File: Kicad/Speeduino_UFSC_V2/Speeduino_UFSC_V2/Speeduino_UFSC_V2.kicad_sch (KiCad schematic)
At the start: 1 part

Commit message: Add pdf
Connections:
- net MCU-A10: no longer names the net of A2.A10
- net MCU-A5: no longer names the net of A2.A5
- net MCU-A6: no longer names the net of A2.A6
- net MCU-A7: no longer names the net of A2.A7
- net MCU-A9: no longer names the net of A2.A9
- net MCU-D10: no longer names the net of A2.D10
- net MCU-D11: no longer names the net of A2.D11
- net MCU-D12: no longer names the net of A2.D12
- net MCU-D13: no longer names the net of A2.D13
- net MCU-D14: no longer names the net of A2.D14 (D14/TX3)
- net MCU-D15: no longer names the net of A2.D15 (D15/RX3)
- net MCU-D20: no longer names the net of A2.D20 (D20/SDA)
- net MCU-D21: no longer names the net of A2.D21 (D21/SCL)
- net MCU-D22: no longer names the net of A2.D22
- net MCU-D23: no longer names the net of A2.D23
- net MCU-D25: no longer names the net of A2.D25
- net MCU-D26: no longer names the net of A2.D26
- net MCU-D27: no longer names the net of A2.D27
- net MCU-D28: no longer names the net of A2.D28
- net MCU-D29: no longer names the net of A2.D29
- net MCU-D30: no longer names the net of A2.D30
- net MCU-D31: no longer names the net of A2.D31
- net MCU-D32: no longer names the net of A2.D32
- net MCU-D33: no longer names the net of A2.D33
- net MCU-D34: no longer names the net of A2.D34
- net MCU-D35: no longer names the net of A2.D35
- net MCU-D36: no longer names the net of A2.D36
- net MCU-D37: no longer names the net of A2.D37
- net MCU-D39: no longer names the net of A2.D39
- net MCU-D41: no longer names the net of A2.D41
- net MCU-D42: no longer names the net of A2.D42
- net MCU-D43: no longer names the net of A2.D43
- net MCU-D44: no longer names the net of A2.D44
- net MCU-D46: no longer names the net of A2.D46
- net MCU-D48: no longer names the net of A2.D48
- net MCU-D50: no longer names the net of A2.D50 (D50_MISO)
- net MCU-D52: no longer names the net of A2.D52 (D52_SCK)
- net MCU-D53: no longer names the net of A2.D53 (D53_CS)
- net MCU-D9: no longer names the net of A2.D9
- net MISO: no longer names the net of A2.MISO (SPI_MISO)
- net MOSI: no longer names the net of A2.MOSI (SPI_MOSI)
- net RESET: no longer names the net of A2.RST1 (RESET)
- net SCLK: no longer names the net of A2.SCK (SPI_SCK)
- no-connect marks 3 -> 55

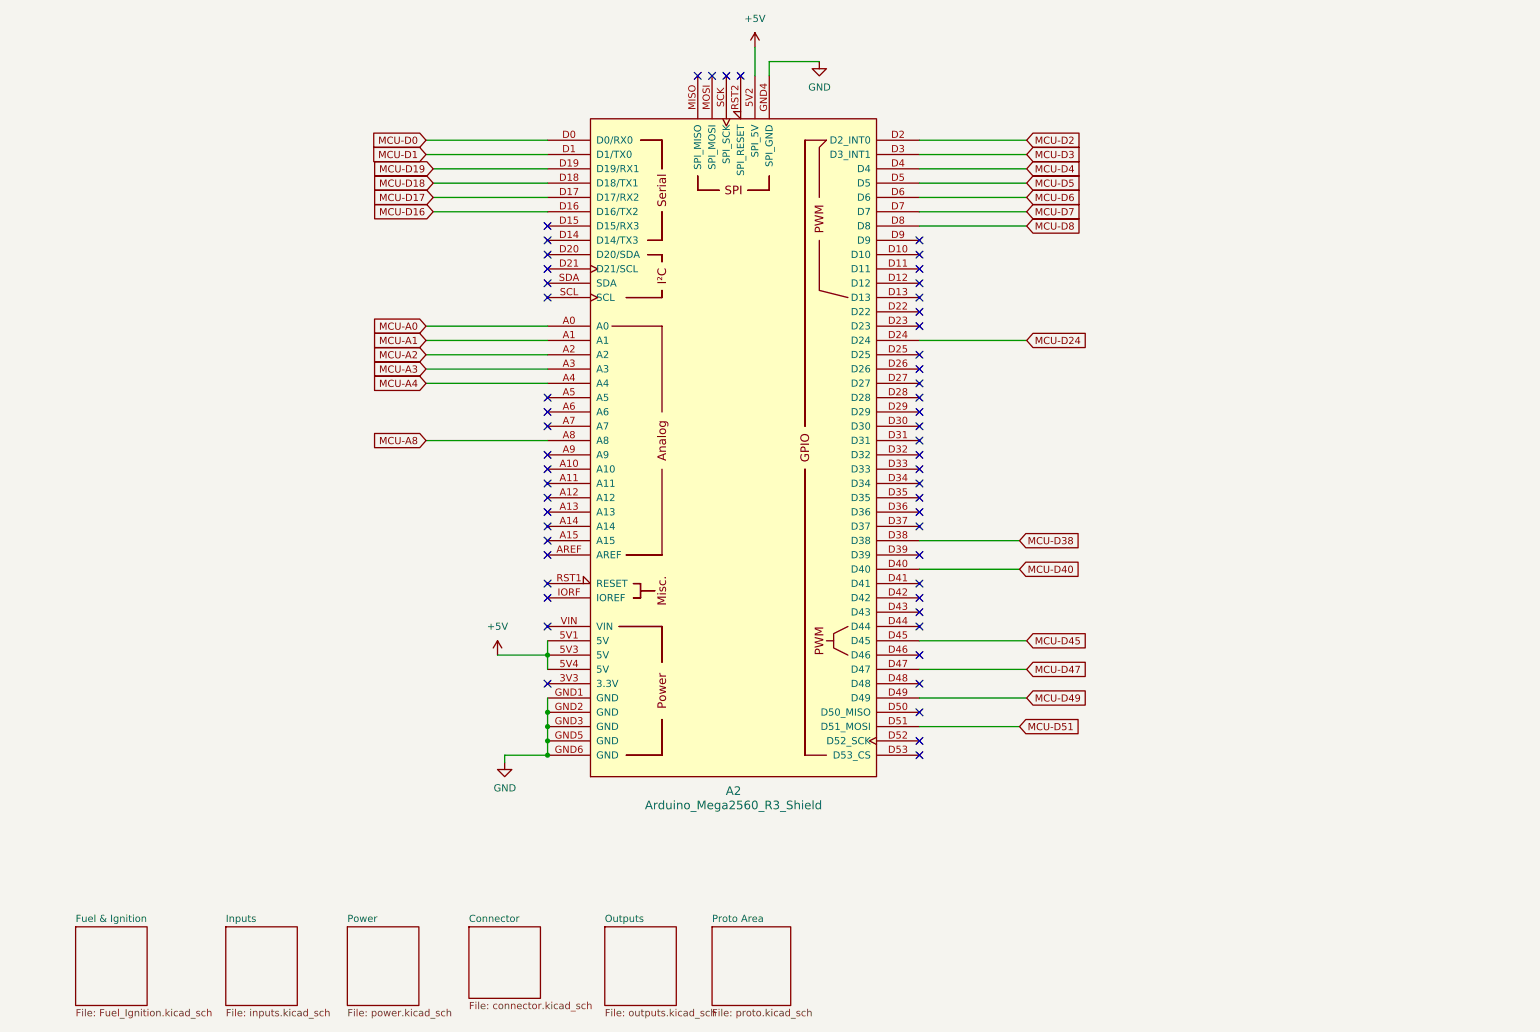
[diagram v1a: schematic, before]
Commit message: Add 2 injectors in schematic
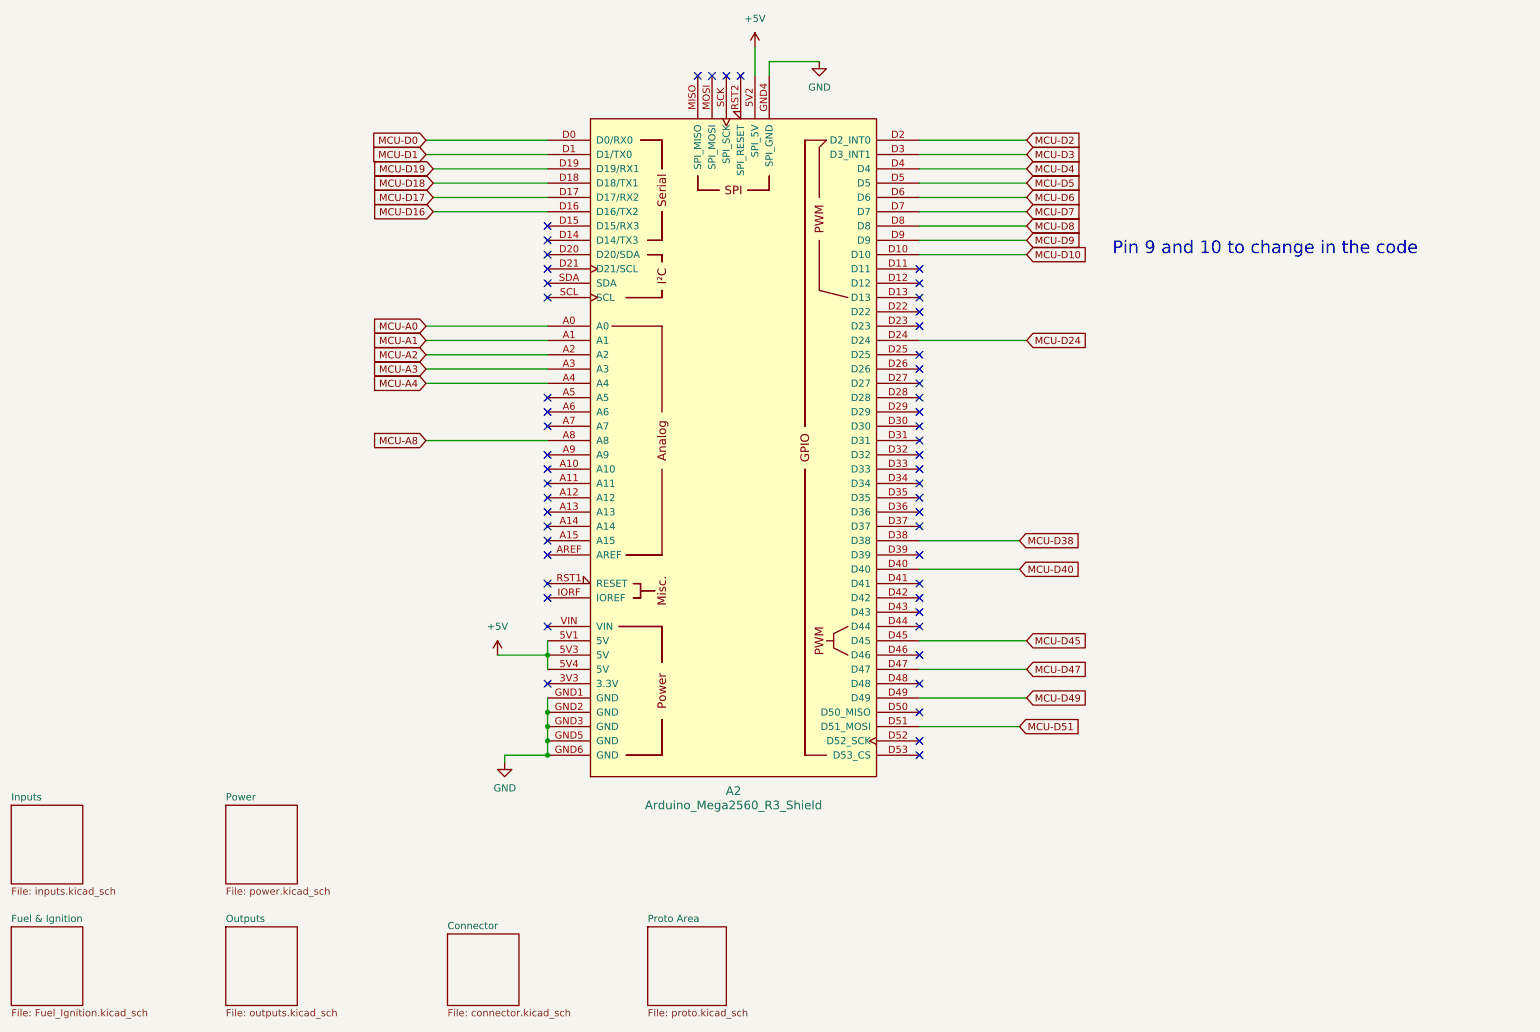
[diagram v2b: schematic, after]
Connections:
- net MCU-D10: now reaches A2.D10
- net MCU-D9: now reaches A2.D9
- no-connect marks 55 -> 53
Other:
- note added: "Pin 9 and 10 to change in the code"
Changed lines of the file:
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@@
-	)
-	(no_connect
-		(at 176.53 55.88)
 	)
 	(no_connect
@@
 	)
 	(no_connect
-		(at 176.53 58.42)
-	)
-	(no_connect
 		(at 176.53 106.68)
 	)
@@
 	(wire
 		(pts
+			(xy 176.53 58.42) (xy 195.58 58.42)
+		)
+		(stroke
+			(width 0)
+			(type default)
+		)
+	)
+	(wire
+		(pts
 			(xy 101.6 129.54) (xy 110.49 129.54)
 		)
@@
 	(wire
 		(pts
+			(xy 176.53 55.88) (xy 195.58 55.88)
+		)
+		(stroke
+			(width 0)
+			(type default)
+		)
+	)
+	(wire
+		(pts
 			(xy 88.9 71.12) (xy 110.49 71.12)
 		)
@@
 		)
 	)
+	(text "Pin 9 and 10 to change in the code"
+		(exclude_from_sim no)
+		(at 210.82 58.674 0)
+		(effects
+			(font
+				(size 2.2606 2.2606)
+			)
+			(justify left bottom)
+		)
+	)
 	(global_label "MCU-D18"
 		(shape input)
@@
 		(property "Intersheetrefs" "${INTERSHEET_REFS}"
 			(at 88.9 71.12 0)
+			(effects
+				(font
+					(size 1.27 1.27)
+				)
+				(hide yes)
+			)
+		)
+	)
+	(global_label "MCU-D10"
+		(shape input)
+		(at 195.58 58.42 0)
+		(effects
+			(font
+				(size 1.27 1.27)
+			)
+			(justify left)
+		)
+		(property "Intersheetrefs" "${INTERSHEET_REFS}"
+			(at 195.58 58.42 0)
+			(effects
+				(font
+					(size 1.27 1.27)
+				)
+				(hide yes)
+			)
+		)
+	)
+	(global_label "MCU-D9"
+		(shape input)
+		(at 195.58 55.88 0)
+		(effects
+			(font
+				(size 1.27 1.27)
+			)
+			(justify left)
+		)
+		(property "Intersheetrefs" "${INTERSHEET_REFS}"
+			(at 195.58 55.88 0)
 			(effects
 				(font
@@
 	)
 	(sheet
-		(at 53.34 177.8)
+		(at 15.24 156.21)
 		(size 12.7 13.97)
 		(fields_autoplaced yes)
@@
 		)
 		(property "Sheetname" "Inputs"
-			(at 53.34 177.0884 0)
+			(at 15.24 155.4984 0)
 			(effects
 				(font
@@
 		)
 		(property "Sheetfile" "inputs.kicad_sch"
-			(at 53.34 192.3546 0)
+			(at 15.24 170.7646 0)
 			(effects
 				(font
@@
 	)
 	(sheet
-		(at 96.52 177.8)
+		(at 92.71 179.07)
 		(size 12.7 12.7)
 		(fields_autoplaced yes)
@@
 		)
 		(property "Sheetname" "Connector"
-			(at 96.52 177.0884 0)
+			(at 92.71 178.3584 0)
 			(effects
 				(font
@@
 		)
 		(property "Sheetfile" "connector.kicad_sch"
-			(at 96.52 191.0846 0)
+			(at 92.71 192.3546 0)
 			(effects
 				(font
@@
 	)
 	(sheet
-		(at 120.65 177.8)
+		(at 53.34 177.8)
 		(size 12.7 13.97)
 		(fields_autoplaced yes)
@@
 		)
 		(property "Sheetname" "Outputs"
-			(at 120.65 177.0884 0)
+			(at 53.34 177.0884 0)
 			(effects
 				(font
@@
 		)
 		(property "Sheetfile" "outputs.kicad_sch"
-			(at 120.65 192.3546 0)
+			(at 53.34 192.3546 0)
 			(effects
 				(font
@@
 	)
 	(sheet
-		(at 26.67 177.8)
+		(at 15.24 177.8)
 		(size 12.7 13.97)
 		(fields_autoplaced yes)
@@
 		)
 		(property "Sheetname" "Fuel & Ignition"
-			(at 26.67 177.0884 0)
+			(at 15.24 177.0884 0)
 			(effects
 				(font
@@
 		)
 		(property "Sheetfile" "Fuel_Ignition.kicad_sch"
-			(at 26.67 192.3546 0)
+			(at 15.24 192.3546 0)
 			(effects
 				(font
@@
 	)
 	(sheet
-		(at 139.7 177.8)
+		(at 128.27 177.8)
 		(size 13.97 13.97)
 		(fields_autoplaced yes)
@@
 		)
 		(property "Sheetname" "Proto Area"
-			(at 139.7 177.0884 0)
+			(at 128.27 177.0884 0)
 			(effects
 				(font
@@
 		)
 		(property "Sheetfile" "proto.kicad_sch"
-			(at 139.7 192.3546 0)
+			(at 128.27 192.3546 0)
 			(effects
 				(font
@@
 	)
 	(sheet
-		(at 74.93 177.8)
+		(at 53.34 156.21)
 		(size 12.7 13.97)
 		(fields_autoplaced yes)
@@
 		)
 		(property "Sheetname" "Power"
-			(at 74.93 177.0884 0)
+			(at 53.34 155.4984 0)
 			(effects
 				(font
@@
 		)
 		(property "Sheetfile" "power.kicad_sch"
-			(at 74.93 192.3546 0)
-			(effects
-				(font
+			(at 53.34 170.7646 0)
+			(effects
+				(font
